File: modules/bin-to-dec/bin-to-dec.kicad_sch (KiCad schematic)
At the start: 4 parts, among them J1 Conn_02x26_Odd_Even

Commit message: using plugin to generate jlc production files
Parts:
- C1, C2, C3: LCSC Part # (none) -> C1590
- J1: now left out of the parts list
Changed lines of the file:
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@@
+			)
+		)
+		(property "LCSC Part #" "C1590"
+			(at 220.98 82.55 0)
+			(effects
+				(font
+					(size 1.27 1.27)
+				)
+				(hide yes)
 			)
 		)
@@
 		(unit 1)
 		(exclude_from_sim no)
-		(in_bom yes)
+		(in_bom no)
 		(on_board yes)
 		(dnp no)
@@
 			)
 		)
+		(property "LCSC Part #" "C1590"
+			(at 210.82 82.55 0)
+			(effects
+				(font
+					(size 1.27 1.27)
+				)
+				(hide yes)
+			)
+		)
 		(pin "2"
 		)
@@
 			(at 199.39 82.55 0)
 			(effects
+				(font
+					(size 1.27 1.27)
+				)
+				(hide yes)
+			)
+		)
+		(property "LCSC Part #" "C1590"
+			(at 199.39 82.55 0)
+			(effects

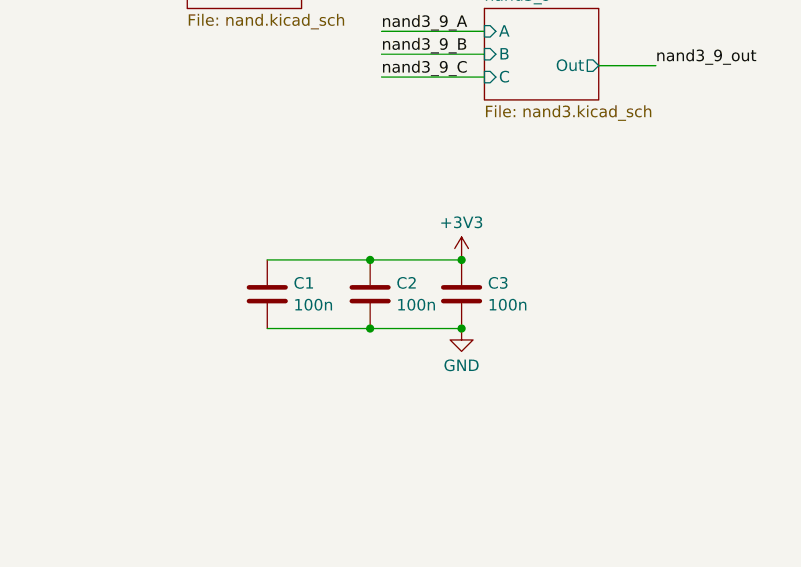
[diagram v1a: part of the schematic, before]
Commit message: move components to top layer :(
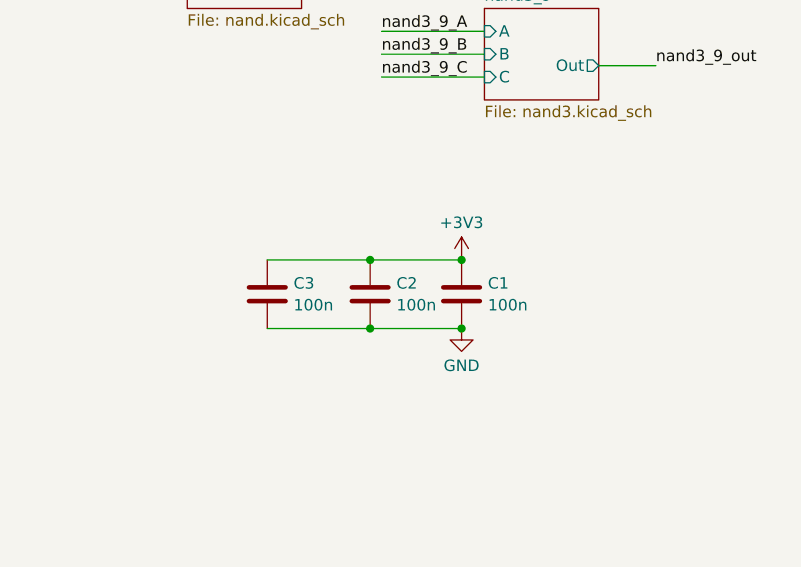
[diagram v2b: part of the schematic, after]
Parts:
- C1: renamed from C3; LCSC part number (none) -> C1590
- C2: LCSC part number (none) -> C1590
- C3: renamed from C1; LCSC part number (none) -> C1590
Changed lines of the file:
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@@
 		(dnp no)
 		(fields_autoplaced yes)
-		(property "Reference" "C3"
+		(property "Reference" "C1"
 			(at 223.901 81.3378 0)
 			(effects
@@
 		)
 		(property "LCSC Part #" "C1590"
+			(at 220.98 82.55 0)
+			(effects
+				(font
+					(size 1.27 1.27)
+				)
+				(hide yes)
+			)
+		)
+		(property "LCSC part number" "C1590"
 			(at 220.98 82.55 0)
 			(effects
@@
 			(project "bin-to-dec"
 				(path "/b244e12b-f85f-4579-ba5e-848643f54694"
-					(reference "C3")
+					(reference "C1")
 					(unit 1)
 				)
@@
 			)
 		)
+		(property "LCSC part number" ""
+			(at 58.42 86.36 0)
+			(effects
+				(font
+					(size 1.27 1.27)
+				)
+				(hide yes)
+			)
+		)
 		(pin "25"
 		)
@@
 			)
 		)
+		(property "LCSC part number" "C1590"
+			(at 210.82 82.55 0)
+			(effects
+				(font
+					(size 1.27 1.27)
+				)
+				(hide yes)
+			)
+		)
 		(pin "2"
 		)
@@
 		(dnp no)
 		(fields_autoplaced yes)
-		(property "Reference" "C1"
+		(property "Reference" "C3"
 			(at 202.311 81.3378 0)
 			(effects
@@
 		)
 		(property "LCSC Part #" "C1590"
+			(at 199.39 82.55 0)
+			(effects
+				(font
+					(size 1.27 1.27)
+				)
+				(hide yes)
+			)
+		)
+		(property "LCSC part number" "C1590"
 			(at 199.39 82.55 0)
 			(effects
@@
 			(project "bin-to-dec"
 				(path "/b244e12b-f85f-4579-ba5e-848643f54694"
-					(reference "C1")
+					(reference "C3")
 					(unit 1)
 				)

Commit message: switched to jlc basic components
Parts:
- C1, C2, C3: LCSC Part # C1590 -> C14663
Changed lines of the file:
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@@
 			)
 		)
-		(property "LCSC Part #" "C1590"
+		(property "LCSC Part #" "C14663"
 			(at 220.98 82.55 0)
 			(effects
@@
 			)
 		)
-		(property "LCSC Part #" "C1590"
+		(property "LCSC Part #" "C14663"
 			(at 210.82 82.55 0)
 			(effects
@@
 			)
 		)
-		(property "LCSC Part #" "C1590"
+		(property "LCSC Part #" "C14663"
 			(at 199.39 82.55 0)
 			(effects

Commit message: minor edits
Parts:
- C1, C2, C3: LCSC part number C1590 -> (none)
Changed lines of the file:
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@@
-			)
-		)
-		(property "LCSC part number" "C1590"
-			(at 220.98 82.55 0)
-			(effects
-				(font
-					(size 1.27 1.27)
-				)
-				(hide yes)
 			)
 		)
@@
 			)
 		)
-		(property "LCSC part number" ""
-			(at 58.42 86.36 0)
-			(effects
-				(font
-					(size 1.27 1.27)
-				)
-				(hide yes)
-			)
-		)
 		(pin "25"
 		)
@@
 			)
 		)
-		(property "LCSC part number" "C1590"
-			(at 210.82 82.55 0)
-			(effects
-				(font
-					(size 1.27 1.27)
-				)
-				(hide yes)
-			)
-		)
 		(pin "2"
 		)
@@
 			(at 199.39 82.55 0)
 			(effects
-				(font
-					(size 1.27 1.27)
-				)
-				(hide yes)
-			)
-		)
-		(property "LCSC part number" "C1590"
-			(at 199.39 82.55 0)
-			(effects
